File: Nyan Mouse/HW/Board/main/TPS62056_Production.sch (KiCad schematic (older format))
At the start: 7 parts, among them U201 TPS6205X

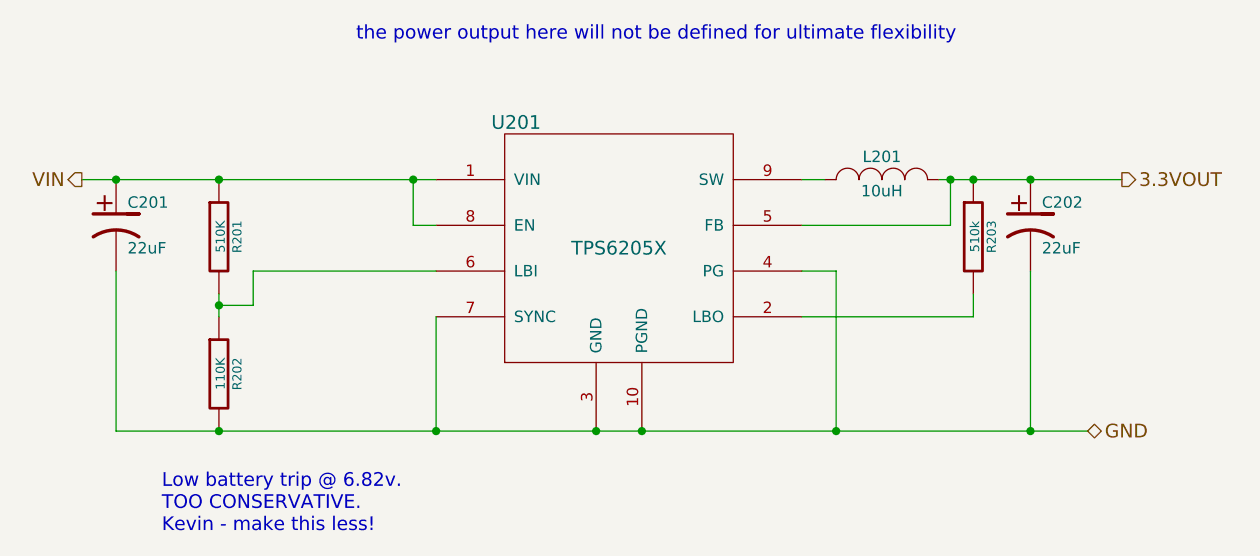
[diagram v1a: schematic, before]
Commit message: Flipped some RGB leds, added emitter pulldowns
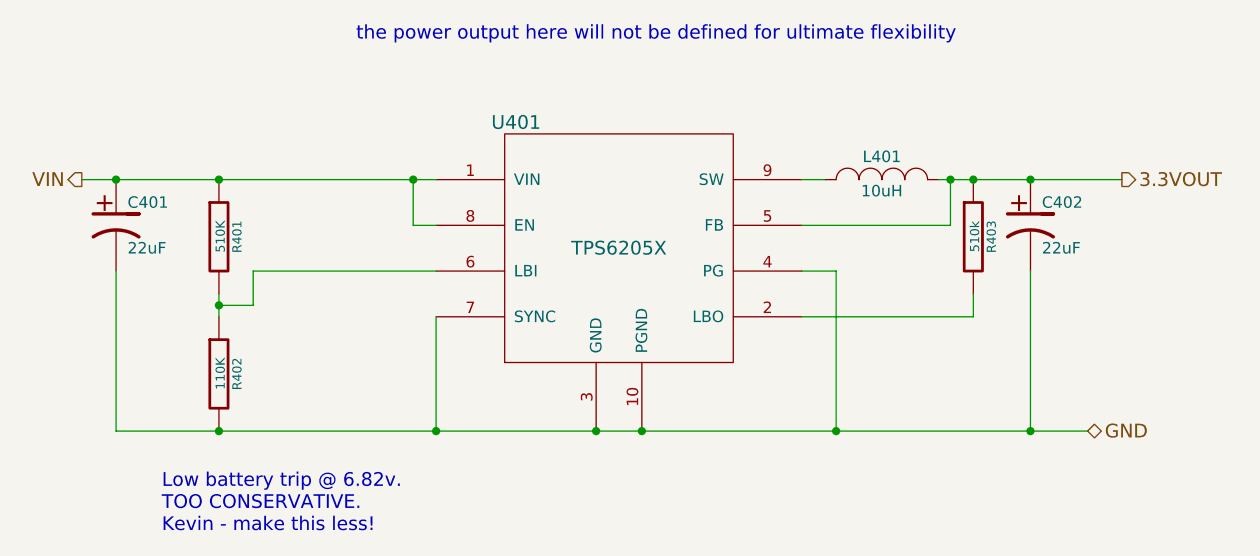
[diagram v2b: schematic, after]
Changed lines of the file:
@@
 LIBS:valves
 LIBS:Nyan Mouse-cache
-EELAYER 24 0
+EELAYER 27 0
 EELAYER END
 $Descr USLetter 11000 8500
@@
 Sheet 4 5
 Title "Nyan Mouse"
-Date "23 Apr 2014"
+Date "24 apr 2014"
 Rev "Alpha"
 Comp "IEEE UCR"
@@
 AR Path="/535488D9/535727C9" Ref="U201"  Part="1"
 AR Path="/53573052/535727C9" Ref="U401"  Part="1"
-F 0 "U201" H 2850 2750 60  0000 C CNN
+F 0 "U401" H 2850 2750 60  0000 C CNN
 F 1 "TPS6205X" H 3300 2200 60  0000 C CNN
 F 2 "" H 2500 2650 60  0000 C CNN
@@
 AR Path="/535488D9/535727CA" Ref="C201"  Part="1"
 AR Path="/53573052/535727CA" Ref="C401"  Part="1"
-F 0 "C201" H 1150 2800 50  0000 L CNN
+F 0 "C401" H 1150 2800 50  0000 L CNN
 F 1 "22uF" H 1150 2600 50  0000 L CNN
 F 2 "" H 1100 2700 60  0000 C CNN
@@
 AR Path="/535488D9/535727CB" Ref="R201"  Part="1"
 AR Path="/53573052/535727CB" Ref="R401"  Part="1"
-F 0 "R201" V 1630 2750 40  0000 C CNN
+F 0 "R401" V 1630 2750 40  0000 C CNN
 F 1 "510K" V 1557 2751 40  0000 C CNN
 F 2 "" V 1480 2750 30  0000 C CNN
@@
 AR Path="/535488D9/535727CC" Ref="R202"  Part="1"
 AR Path="/53573052/535727CC" Ref="R402"  Part="1"
-F 0 "R202" V 1630 3350 40  0000 C CNN
+F 0 "R402" V 1630 3350 40  0000 C CNN
 F 1 "110K" V 1557 3351 40  0000 C CNN
 F 2 "" V 1480 3350 30  0000 C CNN
@@
 AR Path="/535488D9/535727CD" Ref="R203"  Part="1"
 AR Path="/53573052/535727CD" Ref="R403"  Part="1"
-F 0 "R203" V 4930 2750 40  0000 C CNN
+F 0 "R403" V 4930 2750 40  0000 C CNN
 F 1 "510k" V 4857 2751 40  0000 C CNN
 F 2 "" V 4780 2750 30  0000 C CNN
@@
 AR Path="/535488D9/535727CE" Ref="L201"  Part="1"
 AR Path="/53573052/535727CE" Ref="L401"  Part="1"
-F 0 "L201" H 4450 2600 50  0000 C CNN
+F 0 "L401" H 4450 2600 50  0000 C CNN
 F 1 "10uH" H 4450 2450 50  0000 C CNN
 F 2 "" H 4450 2500 60  0000 C CNN
@@
 AR Path="/535488D9/535727CF" Ref="C202"  Part="1"
 AR Path="/53573052/535727CF" Ref="C402"  Part="1"
-F 0 "C202" H 5150 2800 50  0000 L CNN
+F 0 "C402" H 5150 2800 50  0000 L CNN
 F 1 "22uF" H 5150 2600 50  0000 L CNN
 F 2 "" H 5100 2700 60  0000 C CNN
